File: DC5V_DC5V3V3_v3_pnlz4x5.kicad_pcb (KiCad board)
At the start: 2 copper layers, 86 x 95.9 mm, 480 parts, among them J1 Vout1, J2 Vout2, Q1 BSS138, U1 LM1117-3.3

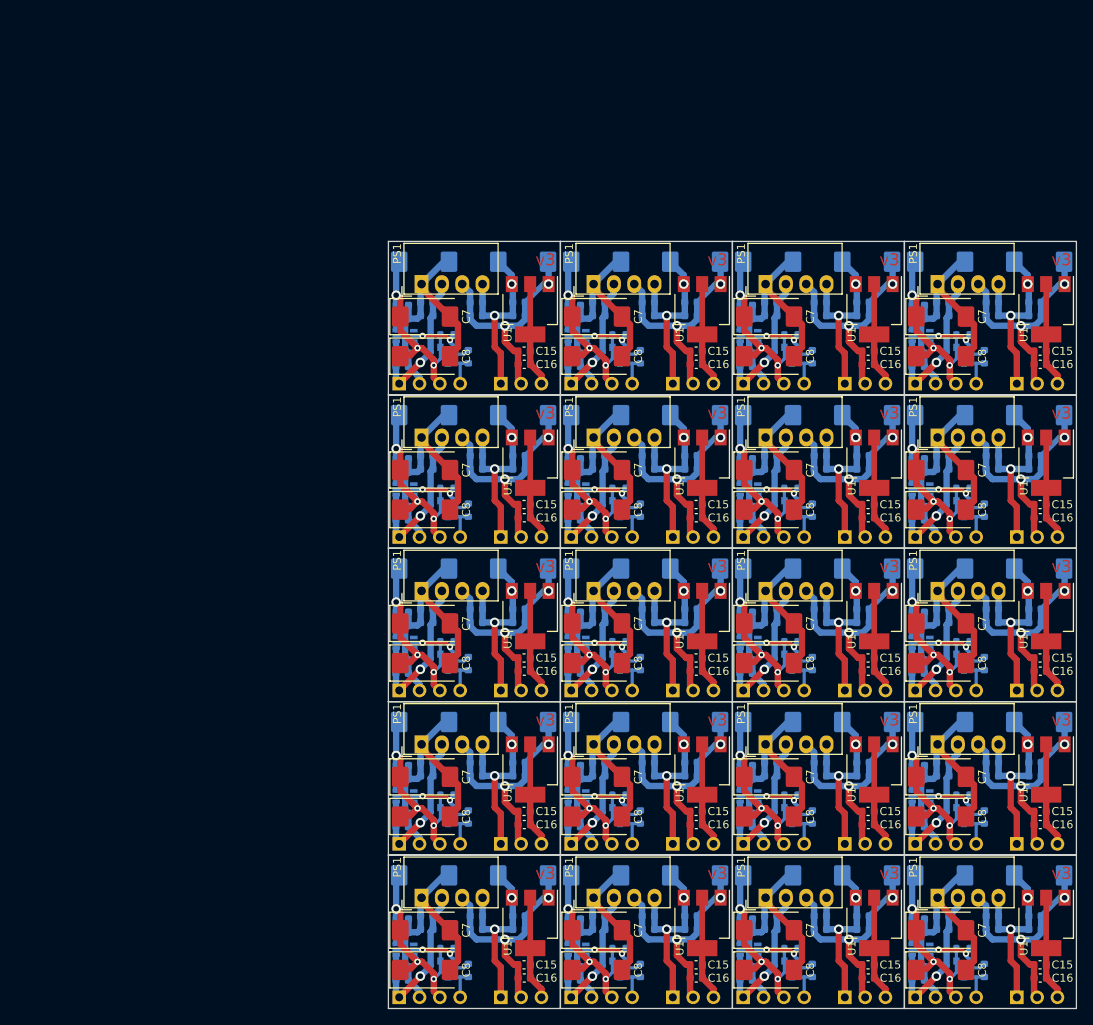
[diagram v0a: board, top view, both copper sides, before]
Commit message: Сформирован перечень элементов, 3D-модель, исправлены ошибки, реализована панелизация платы.
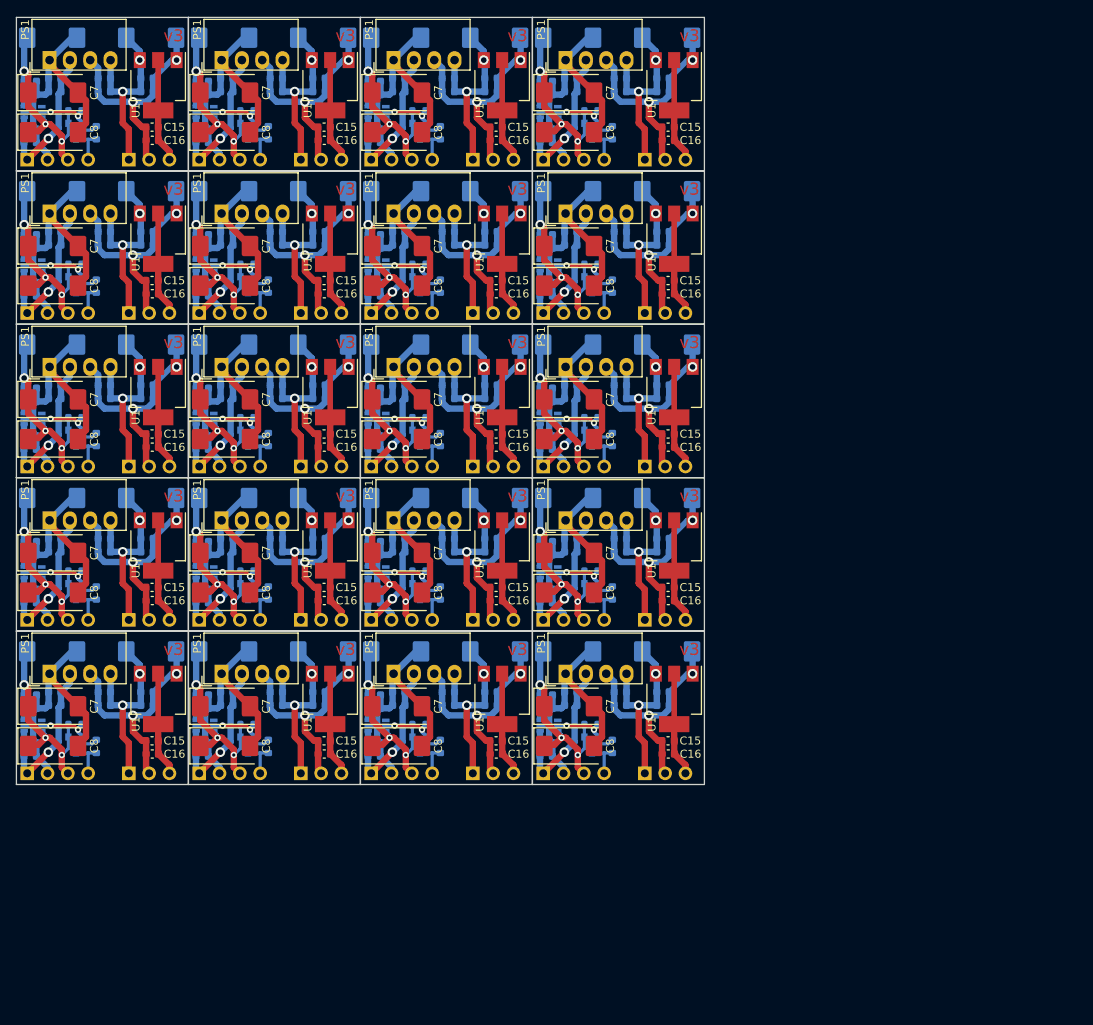
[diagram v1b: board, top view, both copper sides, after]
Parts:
- removed the C1 at (166.2, 163.0)
- removed the C1 at (144.7, 124.6)
- removed the C1 at (123.2, 124.6)
- removed the C1 at (101.7, 124.6)
- removed the C1 at (166.2, 105.4)
- removed the C1 at (144.7, 105.4)
- removed the C1 at (123.2, 105.4)
- removed the C1 at (101.7, 105.4)
- removed the C1 at (166.2, 86.3)
- removed the C1 at (144.7, 86.3)
- removed the C1 at (123.2, 86.3)
- removed the C1 at (144.7, 163.0)
- removed the C1 at (123.2, 163.0)
- removed the C1 at (101.7, 163.0)
- removed the C1 at (166.2, 143.8)
- removed the C1 at (144.7, 143.8)
- removed the C1 at (123.2, 143.8)
- removed the C1 at (101.7, 143.8)
- removed the C1 at (166.2, 124.6)
- removed the C10 at (175.5, 156.6)
- removed the C10 at (154.0, 118.3)
- removed the C10 at (132.5, 118.3)
- removed the C10 at (111.0, 118.3)
- removed the C10 at (175.5, 99.1)
- removed the C10 at (154.0, 99.1)
- removed the C10 at (132.5, 99.1)
- removed the C10 at (111.0, 99.1)
- removed the C10 at (175.5, 79.9)
- removed the C10 at (154.0, 79.9)
- removed the C10 at (132.5, 79.9)
- removed the C10 at (154.0, 156.6)
- removed the C10 at (132.5, 156.6)
- removed the C10 at (111.0, 156.6)
- removed the C10 at (175.5, 137.4)
- removed the C10 at (154.0, 137.4)
- removed the C10 at (132.5, 137.4)
- removed the C10 at (111.0, 137.4)
- removed the C10 at (175.5, 118.3)
- removed the C11 at (169.0, 149.9)
- removed the C11 at (147.5, 111.5)
- removed the C11 at (126.0, 111.5)
- removed the C11 at (104.5, 111.5)
- removed the C11 at (169.0, 92.4)
- removed the C11 at (147.5, 92.4)
- removed the C11 at (126.0, 92.4)
- removed the C11 at (104.5, 92.4)
- removed the C11 at (169.0, 73.2)
- removed the C11 at (147.5, 73.2)
- removed the C11 at (126.0, 73.2)
- removed the C11 at (147.5, 149.9)
- removed the C11 at (126.0, 149.9)
- removed the C11 at (104.5, 149.9)
- removed the C11 at (169.0, 130.7)
- removed the C11 at (147.5, 130.7)
- removed the C11 at (126.0, 130.7)
- removed the C11 at (104.5, 130.7)
- removed the C11 at (169.0, 111.5)
- removed the C12 at (181.3, 149.9)
- removed the C12 at (159.8, 111.5)
- removed the C12 at (138.3, 111.5)
- removed the C12 at (116.8, 111.5)
- removed the C12 at (181.3, 92.4)
- removed the C12 at (159.8, 92.4)
- removed the C12 at (138.3, 92.4)
- removed the C12 at (116.8, 92.4)
- removed the C12 at (181.3, 73.2)
- removed the C12 at (159.8, 73.2)
- removed the C12 at (138.3, 73.2)
- removed the C12 at (159.8, 149.9)
- removed the C12 at (138.3, 149.9)
- removed the C12 at (116.8, 149.9)
- removed the C12 at (181.3, 130.7)
- removed the C12 at (159.8, 130.7)
- removed the C12 at (138.3, 130.7)
- removed the C12 at (116.8, 130.7)
- removed the C12 at (181.3, 111.5)
- removed the C13 at (180.8, 155.0)
- removed the C13 at (159.3, 116.6)
- removed the C13 at (137.8, 116.6)
- removed the C13 at (116.3, 116.6)
- removed the C13 at (180.8, 97.4)
- removed the C13 at (159.3, 97.4)
- removed the C13 at (137.8, 97.4)
- removed the C13 at (116.3, 97.4)
- removed the C13 at (180.8, 78.3)
- removed the C13 at (159.3, 78.3)
- removed the C13 at (137.8, 78.3)
- removed the C13 at (159.3, 155.0)
- removed the C13 at (137.8, 155.0)
- removed the C13 at (116.3, 155.0)
- removed the C13 at (180.8, 135.8)
- removed the C13 at (159.3, 135.8)
- removed the C13 at (137.8, 135.8)
- removed the C13 at (116.3, 135.8)
- removed the C13 at (180.8, 116.6)
- removed the C14 at (180.8, 156.6)
- removed the C14 at (159.3, 118.3)
- removed the C14 at (137.8, 118.3)
- removed the C14 at (116.3, 118.3)
- removed the C14 at (180.8, 99.1)
- removed the C14 at (159.3, 99.1)
- removed the C14 at (137.8, 99.1)
- removed the C14 at (116.3, 99.1)
- removed the C14 at (180.8, 79.9)
- removed the C14 at (159.3, 79.9)
- removed the C14 at (137.8, 79.9)
- removed the C14 at (159.3, 156.6)
- removed the C14 at (137.8, 156.6)
- removed the C14 at (116.3, 156.6)
- removed the C14 at (180.8, 137.4)
- removed the C14 at (159.3, 137.4)
- removed the C14 at (137.8, 137.4)
- removed the C14 at (116.3, 137.4)
- removed the C14 at (180.8, 118.3)
- removed the C15 at (181.5, 161.1)
- removed the C15 at (160.0, 122.7)
- removed the C15 at (138.5, 122.7)
- removed the C15 at (117.0, 122.7)
- removed the C15 at (181.5, 103.5)
- removed the C15 at (160.0, 103.5)
- removed the C15 at (138.5, 103.5)
- removed the C15 at (117.0, 103.5)
- removed the C15 at (181.5, 84.4)
- removed the C15 at (160.0, 84.4)
- removed the C15 at (138.5, 84.4)
- removed the C15 at (160.0, 161.1)
- removed the C15 at (138.5, 161.1)
- removed the C15 at (117.0, 161.1)
- removed the C15 at (181.5, 141.9)
- removed the C15 at (160.0, 141.9)
- removed the C15 at (138.5, 141.9)
- removed the C15 at (117.0, 141.9)
- removed the C15 at (181.5, 122.7)
- removed the C16 at (181.5, 162.7)
- removed the C16 at (160.0, 124.4)
- removed the C16 at (138.5, 124.4)
- removed the C16 at (117.0, 124.4)
- removed the C16 at (181.5, 105.2)
- removed the C16 at (160.0, 105.2)
- removed the C16 at (138.5, 105.2)
- removed the C16 at (117.0, 105.2)
- removed the C16 at (181.5, 86.0)
- removed the C16 at (160.0, 86.0)
- removed the C16 at (138.5, 86.0)
- removed the C16 at (160.0, 162.7)
- removed the C16 at (138.5, 162.7)
- removed the C16 at (117.0, 162.7)
- removed the C16 at (181.5, 143.5)
- removed the C16 at (160.0, 143.5)
- removed the C16 at (138.5, 143.5)
- removed the C16 at (117.0, 143.5)
- removed the C16 at (181.5, 124.4)
- removed the C2 at (169.3, 156.6)
- removed the C2 at (147.8, 118.3)
- removed the C2 at (126.3, 118.3)
- removed the C2 at (104.8, 118.3)
- removed the C2 at (169.3, 99.1)
- removed the C2 at (147.8, 99.1)
- removed the C2 at (126.3, 99.1)
- removed the C2 at (104.8, 99.1)
- removed the C2 at (169.3, 79.9)
- removed the C2 at (147.8, 79.9)
- removed the C2 at (126.3, 79.9)
- removed the C2 at (147.8, 156.6)
- removed the C2 at (126.3, 156.6)
- removed the C2 at (104.8, 156.6)
- removed the C2 at (169.3, 137.4)
- removed the C2 at (147.8, 137.4)
- removed the C2 at (126.3, 137.4)
- removed the C2 at (104.8, 137.4)
- removed the C2 at (169.3, 118.3)
- removed the C3 at (166.2, 161.3)
- removed the C3 at (144.7, 123.0)
- removed the C3 at (123.2, 123.0)
- removed the C3 at (101.7, 123.0)
- removed the C3 at (166.2, 103.8)
- removed the C3 at (144.7, 103.8)
- removed the C3 at (123.2, 103.8)
- removed the C3 at (101.7, 103.8)
- removed the C3 at (166.2, 84.6)
- removed the C3 at (144.7, 84.6)
- removed the C3 at (123.2, 84.6)
- removed the C3 at (144.7, 161.3)
- removed the C3 at (123.2, 161.3)
- removed the C3 at (101.7, 161.3)
- removed the C3 at (166.2, 142.1)
- removed the C3 at (144.7, 142.1)
- removed the C3 at (123.2, 142.1)
- removed the C3 at (101.7, 142.1)
- removed the C3 at (166.2, 123.0)
- removed the C4 at (169.3, 155.0)
- removed the C4 at (147.8, 116.6)
- removed the C4 at (126.3, 116.6)
- removed the C4 at (104.8, 116.6)
- removed the C4 at (169.3, 97.4)
- removed the C4 at (147.8, 97.4)
- removed the C4 at (126.3, 97.4)
- removed the C4 at (104.8, 97.4)
- removed the C4 at (169.3, 78.3)
- removed the C4 at (147.8, 78.3)
- removed the C4 at (126.3, 78.3)
- removed the C4 at (147.8, 155.0)
- removed the C4 at (126.3, 155.0)
- removed the C4 at (104.8, 155.0)
- removed the C4 at (169.3, 135.8)
- removed the C4 at (147.8, 135.8)
- removed the C4 at (126.3, 135.8)
- removed the C4 at (104.8, 135.8)
- removed the C4 at (169.3, 116.6)
- removed the C5 at (166.2, 157.0)
- removed the C5 at (144.7, 118.7)
- removed the C5 at (123.2, 118.7)
- removed the C5 at (101.7, 118.7)
- removed the C5 at (166.2, 99.5)
- removed the C5 at (144.7, 99.5)
- removed the C5 at (123.2, 99.5)
- removed the C5 at (101.7, 99.5)
- removed the C5 at (166.2, 80.3)
- removed the C5 at (144.7, 80.3)
- removed the C5 at (123.2, 80.3)
- removed the C5 at (144.7, 157.0)
- removed the C5 at (123.2, 157.0)
- removed the C5 at (101.7, 157.0)
- removed the C5 at (166.2, 137.8)
- removed the C5 at (144.7, 137.8)
- removed the C5 at (123.2, 137.8)
- removed the C5 at (101.7, 137.8)
- removed the C5 at (166.2, 118.7)
- removed the C6 at (166.2, 155.4)
- removed the C6 at (144.7, 117.0)
- removed the C6 at (123.2, 117.0)
- removed the C6 at (101.7, 117.0)
- removed the C6 at (166.2, 97.8)
- removed the C6 at (144.7, 97.8)
- removed the C6 at (123.2, 97.8)
- removed the C6 at (101.7, 97.8)
- removed the C6 at (166.2, 78.6)
- removed the C6 at (144.7, 78.6)
- removed the C6 at (123.2, 78.6)
- removed the C6 at (144.7, 155.4)
- removed the C6 at (123.2, 155.4)
- removed the C6 at (101.7, 155.4)
- removed the C6 at (166.2, 136.2)
- removed the C6 at (144.7, 136.2)
- removed the C6 at (123.2, 136.2)
- removed the C6 at (101.7, 136.2)
- removed the C6 at (166.2, 117.0)
- removed the C7 at (169.1, 156.8)
- removed the C7 at (147.6, 118.4)
- removed the C7 at (126.1, 118.4)
- removed the C7 at (104.6, 118.4)
- removed the C7 at (169.1, 99.2)
- removed the C7 at (147.6, 99.2)
- removed the C7 at (126.1, 99.2)
- removed the C7 at (104.6, 99.2)
- removed the C7 at (169.1, 80.0)
- removed the C7 at (147.6, 80.0)
- removed the C7 at (126.1, 80.0)
- removed the C7 at (147.6, 156.8)
- removed the C7 at (126.1, 156.8)
- removed the C7 at (104.6, 156.8)
- removed the C7 at (169.1, 137.6)
- removed the C7 at (147.6, 137.6)
- removed the C7 at (126.1, 137.6)
- removed the C7 at (104.6, 137.6)
- removed the C7 at (169.1, 118.4)
- removed the C8 at (169.1, 161.7)
- removed the C8 at (147.6, 123.4)
- removed the C8 at (126.1, 123.4)
- removed the C8 at (104.6, 123.4)
- removed the C8 at (169.1, 104.2)
- removed the C8 at (147.6, 104.2)
- removed the C8 at (126.1, 104.2)
- removed the C8 at (104.6, 104.2)
- removed the C8 at (169.1, 85.0)
- removed the C8 at (147.6, 85.0)
- removed the C8 at (126.1, 85.0)
- removed the C8 at (147.6, 161.7)
- removed the C8 at (126.1, 161.7)
- removed the C8 at (104.6, 161.7)
- removed the C8 at (169.1, 142.5)
- removed the C8 at (147.6, 142.5)
- removed the C8 at (126.1, 142.5)
- removed the C8 at (104.6, 142.5)
- removed the C8 at (169.1, 123.4)
- removed the C9 at (175.5, 155.0)
- removed the C9 at (154.0, 116.6)
- removed the C9 at (132.5, 116.6)
- removed the C9 at (111.0, 116.6)
- removed the C9 at (175.5, 97.4)
- removed the C9 at (154.0, 97.4)
- removed the C9 at (132.5, 97.4)
- removed the C9 at (111.0, 97.4)
- removed the C9 at (175.5, 78.3)
- removed the C9 at (154.0, 78.3)
- removed the C9 at (132.5, 78.3)
- removed the C9 at (154.0, 155.0)
- removed the C9 at (132.5, 155.0)
- removed the C9 at (111.0, 155.0)
- removed the C9 at (175.5, 135.8)
- removed the C9 at (154.0, 135.8)
- removed the C9 at (132.5, 135.8)
- removed the C9 at (111.0, 135.8)
- removed the C9 at (175.5, 116.6)
- removed the D1 at (166.6, 159.2)
- removed the D1 at (145.1, 120.8)
- removed the D1 at (123.6, 120.8)
- removed the D1 at (102.1, 120.8)
- removed the D1 at (166.6, 101.6)
- removed the D1 at (145.1, 101.6)
- removed the D1 at (123.6, 101.6)
- removed the D1 at (102.1, 101.6)
- removed the D1 at (166.6, 82.5)
- removed the D1 at (145.1, 82.5)
- removed the D1 at (123.6, 82.5)
- removed the D1 at (145.1, 159.2)
- removed the D1 at (123.6, 159.2)
- removed the D1 at (102.1, 159.2)
- removed the D1 at (166.6, 140.0)
- removed the D1 at (145.1, 140.0)
- removed the D1 at (123.6, 140.0)
- removed the D1 at (102.1, 140.0)
- removed the D1 at (166.6, 120.8)
- removed the J1 at (165.9, 165.1)
- removed the J1 at (144.4, 126.8)
- removed the J1 at (122.9, 126.8)
- removed the J1 at (101.4, 126.8)
- removed the J1 at (165.9, 107.6)
- removed the J1 at (144.4, 107.6)
- removed the J1 at (122.9, 107.6)
- removed the J1 at (101.4, 107.6)
- removed the J1 at (165.9, 88.4)
- removed the J1 at (144.4, 88.4)
- removed the J1 at (122.9, 88.4)
- removed the J1 at (144.4, 165.1)
- removed the J1 at (122.9, 165.1)
- removed the J1 at (101.4, 165.1)
- removed the J1 at (165.9, 146.0)
- removed the J1 at (144.4, 146.0)
- removed the J1 at (122.9, 146.0)
- removed the J1 at (101.4, 146.0)
- removed the J1 at (165.9, 126.8)
- removed the J2 at (178.6, 165.1)
- removed the J2 at (157.1, 126.8)
- removed the J2 at (135.6, 126.8)
- removed the J2 at (114.1, 126.8)
- removed the J2 at (178.6, 107.6)
- removed the J2 at (157.1, 107.6)
- removed the J2 at (135.6, 107.6)
- removed the J2 at (114.1, 107.6)
- removed the J2 at (178.6, 88.4)
- removed the J2 at (157.1, 88.4)
- removed the J2 at (135.6, 88.4)
- removed the J2 at (157.1, 165.1)
- removed the J2 at (135.6, 165.1)
- removed the J2 at (114.1, 165.1)
- removed the J2 at (178.6, 146.0)
- removed the J2 at (157.1, 146.0)
- removed the J2 at (135.6, 146.0)
- removed the J2 at (114.1, 146.0)
- removed the J2 at (178.6, 126.8)
- removed the PS1 at (168.6, 152.7)
- removed the PS1 at (147.1, 114.3)
- removed the PS1 at (125.6, 114.3)
- removed the PS1 at (104.1, 114.3)
- removed the PS1 at (168.6, 95.2)
- removed the PS1 at (147.1, 95.2)
- removed the PS1 at (125.6, 95.2)
- removed the PS1 at (104.1, 95.2)
- removed the PS1 at (168.6, 76.0)
- removed the PS1 at (147.1, 76.0)
- removed the PS1 at (125.6, 76.0)
- removed the PS1 at (147.1, 152.7)
- removed the PS1 at (125.6, 152.7)
- removed the PS1 at (104.1, 152.7)
- removed the PS1 at (168.6, 133.5)
- removed the PS1 at (147.1, 133.5)
- removed the PS1 at (125.6, 133.5)
- removed the PS1 at (104.1, 133.5)
- removed the PS1 at (168.6, 114.3)
- removed the Q1 at (171.9, 161.6)
- removed the Q1 at (150.4, 123.2)
- removed the Q1 at (128.9, 123.2)
- removed the Q1 at (107.4, 123.2)
- removed the Q1 at (171.9, 104.1)
- removed the Q1 at (150.4, 104.1)
- removed the Q1 at (128.9, 104.1)
- removed the Q1 at (107.4, 104.1)
- removed the Q1 at (171.9, 84.9)
- removed the Q1 at (150.4, 84.9)
- removed the Q1 at (128.9, 84.9)
- removed the Q1 at (150.4, 161.6)
- removed the Q1 at (128.9, 161.6)
- removed the Q1 at (107.4, 161.6)
- removed the Q1 at (171.9, 142.4)
- removed the Q1 at (150.4, 142.4)
- removed the Q1 at (128.9, 142.4)
- removed the Q1 at (107.4, 142.4)
- removed the Q1 at (171.9, 123.2)
- removed the R1 at (171.8, 159.0)
- removed the R1 at (150.3, 120.7)
- removed the R1 at (128.8, 120.7)
- removed the R1 at (107.3, 120.7)
- removed the R1 at (171.8, 101.5)
- removed the R1 at (150.3, 101.5)
- removed the R1 at (128.8, 101.5)
- removed the R1 at (107.3, 101.5)
- removed the R1 at (171.8, 82.3)
- removed the R1 at (150.3, 82.3)
- removed the R1 at (128.8, 82.3)
- removed the R1 at (150.3, 159.0)
- removed the R1 at (128.8, 159.0)
- removed the R1 at (107.3, 159.0)
- removed the R1 at (171.8, 139.9)
- removed the R1 at (150.3, 139.9)
- removed the R1 at (128.8, 139.9)
- removed the R1 at (107.3, 139.9)
- removed the R1 at (171.8, 120.7)
- removed the R2 at (174.5, 161.8)
- removed the R2 at (153.0, 123.4)
- removed the R2 at (131.5, 123.4)
- removed the R2 at (110.0, 123.4)
- removed the R2 at (174.5, 104.2)
- removed the R2 at (153.0, 104.2)
- removed the R2 at (131.5, 104.2)
- removed the R2 at (110.0, 104.2)
- removed the R2 at (174.5, 85.1)
- removed the R2 at (153.0, 85.1)
- removed the R2 at (131.5, 85.1)
- removed the R2 at (153.0, 161.8)
- removed the R2 at (131.5, 161.8)
- removed the R2 at (110.0, 161.8)
- removed the R2 at (174.5, 142.6)
- removed the R2 at (153.0, 142.6)
- removed the R2 at (131.5, 142.6)
- removed the R2 at (110.0, 142.6)
- removed the R2 at (174.5, 123.4)
- removed the U1 at (182.2, 155.8)
- removed the U1 at (160.7, 117.5)
- removed the U1 at (139.2, 117.5)
- removed the U1 at (117.7, 117.5)
- removed the U1 at (182.2, 98.3)
- removed the U1 at (160.7, 98.3)
- removed the U1 at (139.2, 98.3)
- removed the U1 at (117.7, 98.3)
- removed the U1 at (182.2, 79.1)
- removed the U1 at (160.7, 79.1)
- removed the U1 at (139.2, 79.1)
- removed the U1 at (160.7, 155.8)
- removed the U1 at (139.2, 155.8)
- removed the U1 at (117.7, 155.8)
- removed the U1 at (182.2, 136.7)
- removed the U1 at (160.7, 136.7)
- removed the U1 at (139.2, 136.7)
- removed the U1 at (117.7, 136.7)
- removed the U1 at (182.2, 117.5)
- added C1: 10uF, Capacitor_SMD:C_0603_1608Metric, B.Cu at (119.7, 135.0)
- added C1: 10uF, Capacitor_SMD:C_0603_1608Metric, B.Cu at (98.2, 96.6)
- added C1: 10uF, Capacitor_SMD:C_0603_1608Metric, B.Cu at (76.7, 96.6)
- added C1: 10uF, Capacitor_SMD:C_0603_1608Metric, B.Cu at (55.2, 96.6)
- added C1: 10uF, Capacitor_SMD:C_0603_1608Metric, B.Cu at (119.7, 77.4)
- added C1: 10uF, Capacitor_SMD:C_0603_1608Metric, B.Cu at (98.2, 77.4)
- added C1: 10uF, Capacitor_SMD:C_0603_1608Metric, B.Cu at (76.7, 77.4)
- added C1: 10uF, Capacitor_SMD:C_0603_1608Metric, B.Cu at (55.2, 77.4)
- added C1: 10uF, Capacitor_SMD:C_0603_1608Metric, B.Cu at (119.7, 58.3)
- added C1: 10uF, Capacitor_SMD:C_0603_1608Metric, B.Cu at (98.2, 58.3)
- added C1: 10uF, Capacitor_SMD:C_0603_1608Metric, B.Cu at (76.7, 58.3)
- added C1: 10uF, Capacitor_SMD:C_0603_1608Metric, B.Cu at (98.2, 135.0)
- added C1: 10uF, Capacitor_SMD:C_0603_1608Metric, B.Cu at (76.7, 135.0)
- added C1: 10uF, Capacitor_SMD:C_0603_1608Metric, B.Cu at (55.2, 135.0)
- added C1: 10uF, Capacitor_SMD:C_0603_1608Metric, B.Cu at (119.7, 115.8)
- added C1: 10uF, Capacitor_SMD:C_0603_1608Metric, B.Cu at (98.2, 115.8)
- added C1: 10uF, Capacitor_SMD:C_0603_1608Metric, B.Cu at (76.7, 115.8)
- added C1: 10uF, Capacitor_SMD:C_0603_1608Metric, B.Cu at (55.2, 115.8)
- added C1: 10uF, Capacitor_SMD:C_0603_1608Metric, B.Cu at (119.7, 96.6)
- added C10: 10uF, Capacitor_SMD:C_0603_1608Metric, B.Cu at (129.0, 128.6)
- added C10: 10uF, Capacitor_SMD:C_0603_1608Metric, B.Cu at (107.5, 90.3)
- added C10: 10uF, Capacitor_SMD:C_0603_1608Metric, B.Cu at (86.0, 90.3)
- added C10: 10uF, Capacitor_SMD:C_0603_1608Metric, B.Cu at (64.5, 90.3)
- added C10: 10uF, Capacitor_SMD:C_0603_1608Metric, B.Cu at (129.0, 71.1)
- added C10: 10uF, Capacitor_SMD:C_0603_1608Metric, B.Cu at (107.5, 71.1)
- added C10: 10uF, Capacitor_SMD:C_0603_1608Metric, B.Cu at (86.0, 71.1)
- added C10: 10uF, Capacitor_SMD:C_0603_1608Metric, B.Cu at (64.5, 71.1)
- added C10: 10uF, Capacitor_SMD:C_0603_1608Metric, B.Cu at (129.0, 51.9)
- added C10: 10uF, Capacitor_SMD:C_0603_1608Metric, B.Cu at (107.5, 51.9)
- added C10: 10uF, Capacitor_SMD:C_0603_1608Metric, B.Cu at (86.0, 51.9)
- added C10: 10uF, Capacitor_SMD:C_0603_1608Metric, B.Cu at (107.5, 128.6)
- added C10: 10uF, Capacitor_SMD:C_0603_1608Metric, B.Cu at (86.0, 128.6)
- added C10: 10uF, Capacitor_SMD:C_0603_1608Metric, B.Cu at (64.5, 128.6)
- added C10: 10uF, Capacitor_SMD:C_0603_1608Metric, B.Cu at (129.0, 109.4)
- added C10: 10uF, Capacitor_SMD:C_0603_1608Metric, B.Cu at (107.5, 109.4)
- added C10: 10uF, Capacitor_SMD:C_0603_1608Metric, B.Cu at (86.0, 109.4)
- added C10: 10uF, Capacitor_SMD:C_0603_1608Metric, B.Cu at (64.5, 109.4)
- added C10: 10uF, Capacitor_SMD:C_0603_1608Metric, B.Cu at (129.0, 90.3)
- added C11: 470uF, Capacitor_Tantalum_SMD:CP_EIA-7343-15_Kemet-W, B.Cu at (122.5, 121.9)
- added C11: 470uF, Capacitor_Tantalum_SMD:CP_EIA-7343-15_Kemet-W, B.Cu at (101.0, 83.5)
- added C11: 470uF, Capacitor_Tantalum_SMD:CP_EIA-7343-15_Kemet-W, B.Cu at (79.5, 83.5)
- added C11: 470uF, Capacitor_Tantalum_SMD:CP_EIA-7343-15_Kemet-W, B.Cu at (58.0, 83.5)
- added C11: 470uF, Capacitor_Tantalum_SMD:CP_EIA-7343-15_Kemet-W, B.Cu at (122.5, 64.4)
- added C11: 470uF, Capacitor_Tantalum_SMD:CP_EIA-7343-15_Kemet-W, B.Cu at (101.0, 64.4)
- added C11: 470uF, Capacitor_Tantalum_SMD:CP_EIA-7343-15_Kemet-W, B.Cu at (79.5, 64.4)
- added C11: 470uF, Capacitor_Tantalum_SMD:CP_EIA-7343-15_Kemet-W, B.Cu at (58.0, 64.4)
- added C11: 470uF, Capacitor_Tantalum_SMD:CP_EIA-7343-15_Kemet-W, B.Cu at (122.5, 45.2)
- added C11: 470uF, Capacitor_Tantalum_SMD:CP_EIA-7343-15_Kemet-W, B.Cu at (101.0, 45.2)
- added C11: 470uF, Capacitor_Tantalum_SMD:CP_EIA-7343-15_Kemet-W, B.Cu at (79.5, 45.2)
- added C11: 470uF, Capacitor_Tantalum_SMD:CP_EIA-7343-15_Kemet-W, B.Cu at (101.0, 121.9)
- added C11: 470uF, Capacitor_Tantalum_SMD:CP_EIA-7343-15_Kemet-W, B.Cu at (79.5, 121.9)
- added C11: 470uF, Capacitor_Tantalum_SMD:CP_EIA-7343-15_Kemet-W, B.Cu at (58.0, 121.9)
- added C11: 470uF, Capacitor_Tantalum_SMD:CP_EIA-7343-15_Kemet-W, B.Cu at (122.5, 102.7)
- added C11: 470uF, Capacitor_Tantalum_SMD:CP_EIA-7343-15_Kemet-W, B.Cu at (101.0, 102.7)
- added C11: 470uF, Capacitor_Tantalum_SMD:CP_EIA-7343-15_Kemet-W, B.Cu at (79.5, 102.7)
- added C11: 470uF, Capacitor_Tantalum_SMD:CP_EIA-7343-15_Kemet-W, B.Cu at (58.0, 102.7)
- added C11: 470uF, Capacitor_Tantalum_SMD:CP_EIA-7343-15_Kemet-W, B.Cu at (122.5, 83.5)
- added C12: 470uF, Capacitor_Tantalum_SMD:CP_EIA-7343-15_Kemet-W, B.Cu at (134.8, 121.9)
- added C12: 470uF, Capacitor_Tantalum_SMD:CP_EIA-7343-15_Kemet-W, B.Cu at (113.3, 83.5)
- added C12: 470uF, Capacitor_Tantalum_SMD:CP_EIA-7343-15_Kemet-W, B.Cu at (91.8, 83.5)
- added C12: 470uF, Capacitor_Tantalum_SMD:CP_EIA-7343-15_Kemet-W, B.Cu at (70.3, 83.5)
- added C12: 470uF, Capacitor_Tantalum_SMD:CP_EIA-7343-15_Kemet-W, B.Cu at (134.8, 64.4)
- added C12: 470uF, Capacitor_Tantalum_SMD:CP_EIA-7343-15_Kemet-W, B.Cu at (113.3, 64.4)
- added C12: 470uF, Capacitor_Tantalum_SMD:CP_EIA-7343-15_Kemet-W, B.Cu at (91.8, 64.4)
- added C12: 470uF, Capacitor_Tantalum_SMD:CP_EIA-7343-15_Kemet-W, B.Cu at (70.3, 64.4)
- added C12: 470uF, Capacitor_Tantalum_SMD:CP_EIA-7343-15_Kemet-W, B.Cu at (134.8, 45.2)
- added C12: 470uF, Capacitor_Tantalum_SMD:CP_EIA-7343-15_Kemet-W, B.Cu at (113.3, 45.2)
- added C12: 470uF, Capacitor_Tantalum_SMD:CP_EIA-7343-15_Kemet-W, B.Cu at (91.8, 45.2)
- added C12: 470uF, Capacitor_Tantalum_SMD:CP_EIA-7343-15_Kemet-W, B.Cu at (113.3, 121.9)
- added C12: 470uF, Capacitor_Tantalum_SMD:CP_EIA-7343-15_Kemet-W, B.Cu at (91.8, 121.9)
- added C12: 470uF, Capacitor_Tantalum_SMD:CP_EIA-7343-15_Kemet-W, B.Cu at (70.3, 121.9)
- added C12: 470uF, Capacitor_Tantalum_SMD:CP_EIA-7343-15_Kemet-W, B.Cu at (134.8, 102.7)
- added C12: 470uF, Capacitor_Tantalum_SMD:CP_EIA-7343-15_Kemet-W, B.Cu at (113.3, 102.7)
- added C12: 470uF, Capacitor_Tantalum_SMD:CP_EIA-7343-15_Kemet-W, B.Cu at (91.8, 102.7)
- added C12: 470uF, Capacitor_Tantalum_SMD:CP_EIA-7343-15_Kemet-W, B.Cu at (70.3, 102.7)
- added C12: 470uF, Capacitor_Tantalum_SMD:CP_EIA-7343-15_Kemet-W, B.Cu at (134.8, 83.5)
- added C13: 10uF, Capacitor_SMD:C_0603_1608Metric, B.Cu at (134.3, 127.0)
- added C13: 10uF, Capacitor_SMD:C_0603_1608Metric, B.Cu at (112.8, 88.6)
- added C13: 10uF, Capacitor_SMD:C_0603_1608Metric, B.Cu at (91.3, 88.6)
- added C13: 10uF, Capacitor_SMD:C_0603_1608Metric, B.Cu at (69.8, 88.6)
- added C13: 10uF, Capacitor_SMD:C_0603_1608Metric, B.Cu at (134.3, 69.4)
- added C13: 10uF, Capacitor_SMD:C_0603_1608Metric, B.Cu at (112.8, 69.4)
- added C13: 10uF, Capacitor_SMD:C_0603_1608Metric, B.Cu at (91.3, 69.4)
- added C13: 10uF, Capacitor_SMD:C_0603_1608Metric, B.Cu at (69.8, 69.4)
- added C13: 10uF, Capacitor_SMD:C_0603_1608Metric, B.Cu at (134.3, 50.3)
- added C13: 10uF, Capacitor_SMD:C_0603_1608Metric, B.Cu at (112.8, 50.3)
- added C13: 10uF, Capacitor_SMD:C_0603_1608Metric, B.Cu at (91.3, 50.3)
- added C13: 10uF, Capacitor_SMD:C_0603_1608Metric, B.Cu at (112.8, 127.0)
- added C13: 10uF, Capacitor_SMD:C_0603_1608Metric, B.Cu at (91.3, 127.0)
- added C13: 10uF, Capacitor_SMD:C_0603_1608Metric, B.Cu at (69.8, 127.0)
- added C13: 10uF, Capacitor_SMD:C_0603_1608Metric, B.Cu at (134.3, 107.8)
- added C13: 10uF, Capacitor_SMD:C_0603_1608Metric, B.Cu at (112.8, 107.8)
- added C13: 10uF, Capacitor_SMD:C_0603_1608Metric, B.Cu at (91.3, 107.8)
- added C13: 10uF, Capacitor_SMD:C_0603_1608Metric, B.Cu at (69.8, 107.8)
- added C13: 10uF, Capacitor_SMD:C_0603_1608Metric, B.Cu at (134.3, 88.6)
- added C14: 100nF, Capacitor_SMD:C_0603_1608Metric, B.Cu at (134.3, 128.6)
- added C14: 100nF, Capacitor_SMD:C_0603_1608Metric, B.Cu at (112.8, 90.3)
- added C14: 100nF, Capacitor_SMD:C_0603_1608Metric, B.Cu at (91.3, 90.3)
- added C14: 100nF, Capacitor_SMD:C_0603_1608Metric, B.Cu at (69.8, 90.3)
- added C14: 100nF, Capacitor_SMD:C_0603_1608Metric, B.Cu at (134.3, 71.1)
- added C14: 100nF, Capacitor_SMD:C_0603_1608Metric, B.Cu at (112.8, 71.1)
- added C14: 100nF, Capacitor_SMD:C_0603_1608Metric, B.Cu at (91.3, 71.1)
- added C14: 100nF, Capacitor_SMD:C_0603_1608Metric, B.Cu at (69.8, 71.1)
- added C14: 100nF, Capacitor_SMD:C_0603_1608Metric, B.Cu at (134.3, 51.9)
- added C14: 100nF, Capacitor_SMD:C_0603_1608Metric, B.Cu at (112.8, 51.9)
- added C14: 100nF, Capacitor_SMD:C_0603_1608Metric, B.Cu at (91.3, 51.9)
- added C14: 100nF, Capacitor_SMD:C_0603_1608Metric, B.Cu at (112.8, 128.6)
- added C14: 100nF, Capacitor_SMD:C_0603_1608Metric, B.Cu at (91.3, 128.6)
- added C14: 100nF, Capacitor_SMD:C_0603_1608Metric, B.Cu at (69.8, 128.6)
- added C14: 100nF, Capacitor_SMD:C_0603_1608Metric, B.Cu at (134.3, 109.4)
- added C14: 100nF, Capacitor_SMD:C_0603_1608Metric, B.Cu at (112.8, 109.4)
- added C14: 100nF, Capacitor_SMD:C_0603_1608Metric, B.Cu at (91.3, 109.4)
- added C14: 100nF, Capacitor_SMD:C_0603_1608Metric, B.Cu at (69.8, 109.4)
- added C14: 100nF, Capacitor_SMD:C_0603_1608Metric, B.Cu at (134.3, 90.3)
- added C15: 100nF, Capacitor_SMD:C_0603_1608Metric, F.Cu at (135.0, 133.1)
- added C15: 100nF, Capacitor_SMD:C_0603_1608Metric, F.Cu at (113.5, 94.7)
- added C15: 100nF, Capacitor_SMD:C_0603_1608Metric, F.Cu at (92.0, 94.7)
- added C15: 100nF, Capacitor_SMD:C_0603_1608Metric, F.Cu at (70.5, 94.7)
- added C15: 100nF, Capacitor_SMD:C_0603_1608Metric, F.Cu at (135.0, 75.5)
- added C15: 100nF, Capacitor_SMD:C_0603_1608Metric, F.Cu at (113.5, 75.5)
- added C15: 100nF, Capacitor_SMD:C_0603_1608Metric, F.Cu at (92.0, 75.5)
- added C15: 100nF, Capacitor_SMD:C_0603_1608Metric, F.Cu at (70.5, 75.5)
- added C15: 100nF, Capacitor_SMD:C_0603_1608Metric, F.Cu at (135.0, 56.4)
- added C15: 100nF, Capacitor_SMD:C_0603_1608Metric, F.Cu at (113.5, 56.4)
- added C15: 100nF, Capacitor_SMD:C_0603_1608Metric, F.Cu at (92.0, 56.4)
- added C15: 100nF, Capacitor_SMD:C_0603_1608Metric, F.Cu at (113.5, 133.1)
- added C15: 100nF, Capacitor_SMD:C_0603_1608Metric, F.Cu at (92.0, 133.1)
- added C15: 100nF, Capacitor_SMD:C_0603_1608Metric, F.Cu at (70.5, 133.1)
- added C15: 100nF, Capacitor_SMD:C_0603_1608Metric, F.Cu at (135.0, 113.9)
- added C15: 100nF, Capacitor_SMD:C_0603_1608Metric, F.Cu at (113.5, 113.9)
- added C15: 100nF, Capacitor_SMD:C_0603_1608Metric, F.Cu at (92.0, 113.9)
- added C15: 100nF, Capacitor_SMD:C_0603_1608Metric, F.Cu at (70.5, 113.9)
- added C15: 100nF, Capacitor_SMD:C_0603_1608Metric, F.Cu at (135.0, 94.7)
- added C16: 10uF, Capacitor_SMD:C_0603_1608Metric, F.Cu at (135.0, 134.7)
- added C16: 10uF, Capacitor_SMD:C_0603_1608Metric, F.Cu at (113.5, 96.4)
- added C16: 10uF, Capacitor_SMD:C_0603_1608Metric, F.Cu at (92.0, 96.4)
- added C16: 10uF, Capacitor_SMD:C_0603_1608Metric, F.Cu at (70.5, 96.4)
- added C16: 10uF, Capacitor_SMD:C_0603_1608Metric, F.Cu at (135.0, 77.2)
- added C16: 10uF, Capacitor_SMD:C_0603_1608Metric, F.Cu at (113.5, 77.2)
- added C16: 10uF, Capacitor_SMD:C_0603_1608Metric, F.Cu at (92.0, 77.2)
- added C16: 10uF, Capacitor_SMD:C_0603_1608Metric, F.Cu at (70.5, 77.2)
- added C16: 10uF, Capacitor_SMD:C_0603_1608Metric, F.Cu at (135.0, 58.0)
- added C16: 10uF, Capacitor_SMD:C_0603_1608Metric, F.Cu at (113.5, 58.0)
- added C16: 10uF, Capacitor_SMD:C_0603_1608Metric, F.Cu at (92.0, 58.0)
- added C16: 10uF, Capacitor_SMD:C_0603_1608Metric, F.Cu at (113.5, 134.7)
- added C16: 10uF, Capacitor_SMD:C_0603_1608Metric, F.Cu at (92.0, 134.7)
- added C16: 10uF, Capacitor_SMD:C_0603_1608Metric, F.Cu at (70.5, 134.7)
- added C16: 10uF, Capacitor_SMD:C_0603_1608Metric, F.Cu at (135.0, 115.5)
- added C16: 10uF, Capacitor_SMD:C_0603_1608Metric, F.Cu at (113.5, 115.5)
- added C16: 10uF, Capacitor_SMD:C_0603_1608Metric, F.Cu at (92.0, 115.5)
- added C16: 10uF, Capacitor_SMD:C_0603_1608Metric, F.Cu at (70.5, 115.5)
- added C16: 10uF, Capacitor_SMD:C_0603_1608Metric, F.Cu at (135.0, 96.4)
- added C2: 10uF, Capacitor_SMD:C_0603_1608Metric, B.Cu at (122.8, 128.6)
- added C2: 10uF, Capacitor_SMD:C_0603_1608Metric, B.Cu at (101.3, 90.3)
- added C2: 10uF, Capacitor_SMD:C_0603_1608Metric, B.Cu at (79.8, 90.3)
- added C2: 10uF, Capacitor_SMD:C_0603_1608Metric, B.Cu at (58.3, 90.3)
- added C2: 10uF, Capacitor_SMD:C_0603_1608Metric, B.Cu at (122.8, 71.1)
- added C2: 10uF, Capacitor_SMD:C_0603_1608Metric, B.Cu at (101.3, 71.1)
- added C2: 10uF, Capacitor_SMD:C_0603_1608Metric, B.Cu at (79.8, 71.1)
- added C2: 10uF, Capacitor_SMD:C_0603_1608Metric, B.Cu at (58.3, 71.1)
- added C2: 10uF, Capacitor_SMD:C_0603_1608Metric, B.Cu at (122.8, 51.9)
- added C2: 10uF, Capacitor_SMD:C_0603_1608Metric, B.Cu at (101.3, 51.9)
- added C2: 10uF, Capacitor_SMD:C_0603_1608Metric, B.Cu at (79.8, 51.9)
- added C2: 10uF, Capacitor_SMD:C_0603_1608Metric, B.Cu at (101.3, 128.6)
- added C2: 10uF, Capacitor_SMD:C_0603_1608Metric, B.Cu at (79.8, 128.6)
- added C2: 10uF, Capacitor_SMD:C_0603_1608Metric, B.Cu at (58.3, 128.6)
- added C2: 10uF, Capacitor_SMD:C_0603_1608Metric, B.Cu at (122.8, 109.4)
- added C2: 10uF, Capacitor_SMD:C_0603_1608Metric, B.Cu at (101.3, 109.4)
- added C2: 10uF, Capacitor_SMD:C_0603_1608Metric, B.Cu at (79.8, 109.4)
- added C2: 10uF, Capacitor_SMD:C_0603_1608Metric, B.Cu at (58.3, 109.4)
- added C2: 10uF, Capacitor_SMD:C_0603_1608Metric, B.Cu at (122.8, 90.3)
- added C3: 100nF, Capacitor_SMD:C_0603_1608Metric, B.Cu at (119.7, 133.3)
- added C3: 100nF, Capacitor_SMD:C_0603_1608Metric, B.Cu at (98.2, 95.0)
- added C3: 100nF, Capacitor_SMD:C_0603_1608Metric, B.Cu at (76.7, 95.0)
- added C3: 100nF, Capacitor_SMD:C_0603_1608Metric, B.Cu at (55.2, 95.0)
- added C3: 100nF, Capacitor_SMD:C_0603_1608Metric, B.Cu at (119.7, 75.8)
- added C3: 100nF, Capacitor_SMD:C_0603_1608Metric, B.Cu at (98.2, 75.8)
- added C3: 100nF, Capacitor_SMD:C_0603_1608Metric, B.Cu at (76.7, 75.8)
- added C3: 100nF, Capacitor_SMD:C_0603_1608Metric, B.Cu at (55.2, 75.8)
- added C3: 100nF, Capacitor_SMD:C_0603_1608Metric, B.Cu at (119.7, 56.6)
- added C3: 100nF, Capacitor_SMD:C_0603_1608Metric, B.Cu at (98.2, 56.6)
- added C3: 100nF, Capacitor_SMD:C_0603_1608Metric, B.Cu at (76.7, 56.6)
- added C3: 100nF, Capacitor_SMD:C_0603_1608Metric, B.Cu at (98.2, 133.3)
- added C3: 100nF, Capacitor_SMD:C_0603_1608Metric, B.Cu at (76.7, 133.3)
- added C3: 100nF, Capacitor_SMD:C_0603_1608Metric, B.Cu at (55.2, 133.3)
- added C3: 100nF, Capacitor_SMD:C_0603_1608Metric, B.Cu at (119.7, 114.1)
- added C3: 100nF, Capacitor_SMD:C_0603_1608Metric, B.Cu at (98.2, 114.1)
- added C3: 100nF, Capacitor_SMD:C_0603_1608Metric, B.Cu at (76.7, 114.1)
- added C3: 100nF, Capacitor_SMD:C_0603_1608Metric, B.Cu at (55.2, 114.1)
- added C3: 100nF, Capacitor_SMD:C_0603_1608Metric, B.Cu at (119.7, 95.0)
- added C4: 100nF, Capacitor_SMD:C_0603_1608Metric, B.Cu at (122.8, 127.0)
- added C4: 100nF, Capacitor_SMD:C_0603_1608Metric, B.Cu at (101.3, 88.6)
- added C4: 100nF, Capacitor_SMD:C_0603_1608Metric, B.Cu at (79.8, 88.6)
- added C4: 100nF, Capacitor_SMD:C_0603_1608Metric, B.Cu at (58.3, 88.6)
- added C4: 100nF, Capacitor_SMD:C_0603_1608Metric, B.Cu at (122.8, 69.4)
- added C4: 100nF, Capacitor_SMD:C_0603_1608Metric, B.Cu at (101.3, 69.4)
- added C4: 100nF, Capacitor_SMD:C_0603_1608Metric, B.Cu at (79.8, 69.4)
- added C4: 100nF, Capacitor_SMD:C_0603_1608Metric, B.Cu at (58.3, 69.4)
- added C4: 100nF, Capacitor_SMD:C_0603_1608Metric, B.Cu at (122.8, 50.3)
- added C4: 100nF, Capacitor_SMD:C_0603_1608Metric, B.Cu at (101.3, 50.3)
- added C4: 100nF, Capacitor_SMD:C_0603_1608Metric, B.Cu at (79.8, 50.3)
- added C4: 100nF, Capacitor_SMD:C_0603_1608Metric, B.Cu at (101.3, 127.0)
- added C4: 100nF, Capacitor_SMD:C_0603_1608Metric, B.Cu at (79.8, 127.0)
- added C4: 100nF, Capacitor_SMD:C_0603_1608Metric, B.Cu at (58.3, 127.0)
- added C4: 100nF, Capacitor_SMD:C_0603_1608Metric, B.Cu at (122.8, 107.8)
- added C4: 100nF, Capacitor_SMD:C_0603_1608Metric, B.Cu at (101.3, 107.8)
- added C4: 100nF, Capacitor_SMD:C_0603_1608Metric, B.Cu at (79.8, 107.8)
- added C4: 100nF, Capacitor_SMD:C_0603_1608Metric, B.Cu at (58.3, 107.8)
- added C4: 100nF, Capacitor_SMD:C_0603_1608Metric, B.Cu at (122.8, 88.6)
- added C5: 100nF, Capacitor_SMD:C_0603_1608Metric, B.Cu at (119.7, 129.0)
- added C5: 100nF, Capacitor_SMD:C_0603_1608Metric, B.Cu at (98.2, 90.7)
- added C5: 100nF, Capacitor_SMD:C_0603_1608Metric, B.Cu at (76.7, 90.7)
- added C5: 100nF, Capacitor_SMD:C_0603_1608Metric, B.Cu at (55.2, 90.7)
- added C5: 100nF, Capacitor_SMD:C_0603_1608Metric, B.Cu at (119.7, 71.5)
- added C5: 100nF, Capacitor_SMD:C_0603_1608Metric, B.Cu at (98.2, 71.5)
- added C5: 100nF, Capacitor_SMD:C_0603_1608Metric, B.Cu at (76.7, 71.5)
- added C5: 100nF, Capacitor_SMD:C_0603_1608Metric, B.Cu at (55.2, 71.5)
- added C5: 100nF, Capacitor_SMD:C_0603_1608Metric, B.Cu at (119.7, 52.3)
- added C5: 100nF, Capacitor_SMD:C_0603_1608Metric, B.Cu at (98.2, 52.3)
- added C5: 100nF, Capacitor_SMD:C_0603_1608Metric, B.Cu at (76.7, 52.3)
- added C5: 100nF, Capacitor_SMD:C_0603_1608Metric, B.Cu at (98.2, 129.0)
- added C5: 100nF, Capacitor_SMD:C_0603_1608Metric, B.Cu at (76.7, 129.0)
- added C5: 100nF, Capacitor_SMD:C_0603_1608Metric, B.Cu at (55.2, 129.0)
- added C5: 100nF, Capacitor_SMD:C_0603_1608Metric, B.Cu at (119.7, 109.8)
- added C5: 100nF, Capacitor_SMD:C_0603_1608Metric, B.Cu at (98.2, 109.8)
- added C5: 100nF, Capacitor_SMD:C_0603_1608Metric, B.Cu at (76.7, 109.8)
- added C5: 100nF, Capacitor_SMD:C_0603_1608Metric, B.Cu at (55.2, 109.8)
- added C5: 100nF, Capacitor_SMD:C_0603_1608Metric, B.Cu at (119.7, 90.7)
- added C6: 10uF, Capacitor_SMD:C_0603_1608Metric, B.Cu at (119.7, 127.4)
- added C6: 10uF, Capacitor_SMD:C_0603_1608Metric, B.Cu at (98.2, 89.0)
- added C6: 10uF, Capacitor_SMD:C_0603_1608Metric, B.Cu at (76.7, 89.0)
- added C6: 10uF, Capacitor_SMD:C_0603_1608Metric, B.Cu at (55.2, 89.0)
- added C6: 10uF, Capacitor_SMD:C_0603_1608Metric, B.Cu at (119.7, 69.8)
- added C6: 10uF, Capacitor_SMD:C_0603_1608Metric, B.Cu at (98.2, 69.8)
- added C6: 10uF, Capacitor_SMD:C_0603_1608Metric, B.Cu at (76.7, 69.8)
- added C6: 10uF, Capacitor_SMD:C_0603_1608Metric, B.Cu at (55.2, 69.8)
- added C6: 10uF, Capacitor_SMD:C_0603_1608Metric, B.Cu at (119.7, 50.6)
- added C6: 10uF, Capacitor_SMD:C_0603_1608Metric, B.Cu at (98.2, 50.6)
- added C6: 10uF, Capacitor_SMD:C_0603_1608Metric, B.Cu at (76.7, 50.6)
- added C6: 10uF, Capacitor_SMD:C_0603_1608Metric, B.Cu at (98.2, 127.4)
- added C6: 10uF, Capacitor_SMD:C_0603_1608Metric, B.Cu at (76.7, 127.4)
- added C6: 10uF, Capacitor_SMD:C_0603_1608Metric, B.Cu at (55.2, 127.4)
- added C6: 10uF, Capacitor_SMD:C_0603_1608Metric, B.Cu at (119.7, 108.2)
- added C6: 10uF, Capacitor_SMD:C_0603_1608Metric, B.Cu at (98.2, 108.2)
- added C6: 10uF, Capacitor_SMD:C_0603_1608Metric, B.Cu at (76.7, 108.2)
- added C6: 10uF, Capacitor_SMD:C_0603_1608Metric, B.Cu at (55.2, 108.2)
- added C6: 10uF, Capacitor_SMD:C_0603_1608Metric, B.Cu at (119.7, 89.0)
- added C7: 470uF, Capacitor_Tantalum_SMD:CP_EIA-7343-31_Kemet-D, F.Cu at (122.6, 128.8)
- added C7: 470uF, Capacitor_Tantalum_SMD:CP_EIA-7343-31_Kemet-D, F.Cu at (101.1, 90.4)
- added C7: 470uF, Capacitor_Tantalum_SMD:CP_EIA-7343-31_Kemet-D, F.Cu at (79.6, 90.4)
- added C7: 470uF, Capacitor_Tantalum_SMD:CP_EIA-7343-31_Kemet-D, F.Cu at (58.1, 90.4)
- added C7: 470uF, Capacitor_Tantalum_SMD:CP_EIA-7343-31_Kemet-D, F.Cu at (122.6, 71.2)
- added C7: 470uF, Capacitor_Tantalum_SMD:CP_EIA-7343-31_Kemet-D, F.Cu at (101.1, 71.2)
- added C7: 470uF, Capacitor_Tantalum_SMD:CP_EIA-7343-31_Kemet-D, F.Cu at (79.6, 71.2)
- added C7: 470uF, Capacitor_Tantalum_SMD:CP_EIA-7343-31_Kemet-D, F.Cu at (58.1, 71.2)
- added C7: 470uF, Capacitor_Tantalum_SMD:CP_EIA-7343-31_Kemet-D, F.Cu at (122.6, 52.0)
- added C7: 470uF, Capacitor_Tantalum_SMD:CP_EIA-7343-31_Kemet-D, F.Cu at (101.1, 52.0)
- added C7: 470uF, Capacitor_Tantalum_SMD:CP_EIA-7343-31_Kemet-D, F.Cu at (79.6, 52.0)
- added C7: 470uF, Capacitor_Tantalum_SMD:CP_EIA-7343-31_Kemet-D, F.Cu at (101.1, 128.8)
- added C7: 470uF, Capacitor_Tantalum_SMD:CP_EIA-7343-31_Kemet-D, F.Cu at (79.6, 128.8)
- added C7: 470uF, Capacitor_Tantalum_SMD:CP_EIA-7343-31_Kemet-D, F.Cu at (58.1, 128.8)
- added C7: 470uF, Capacitor_Tantalum_SMD:CP_EIA-7343-31_Kemet-D, F.Cu at (122.6, 109.6)
- added C7: 470uF, Capacitor_Tantalum_SMD:CP_EIA-7343-31_Kemet-D, F.Cu at (101.1, 109.6)
- added C7: 470uF, Capacitor_Tantalum_SMD:CP_EIA-7343-31_Kemet-D, F.Cu at (79.6, 109.6)
- added C7: 470uF, Capacitor_Tantalum_SMD:CP_EIA-7343-31_Kemet-D, F.Cu at (58.1, 109.6)
- added C7: 470uF, Capacitor_Tantalum_SMD:CP_EIA-7343-31_Kemet-D, F.Cu at (122.6, 90.4)
- added C8: 470uF, Capacitor_Tantalum_SMD:CP_EIA-7343-31_Kemet-D, F.Cu at (122.6, 133.7)
- added C8: 470uF, Capacitor_Tantalum_SMD:CP_EIA-7343-31_Kemet-D, F.Cu at (101.1, 95.4)
- added C8: 470uF, Capacitor_Tantalum_SMD:CP_EIA-7343-31_Kemet-D, F.Cu at (79.6, 95.4)
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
